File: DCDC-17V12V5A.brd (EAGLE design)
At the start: 40 x 23 mm, 36 parts, among them CN2 2828XX-2282834-2, CN3 2828XX-2282834-2, Q10 NMOSFET, Q9 NMOSFET, U1 LM3150MHX/NOPB

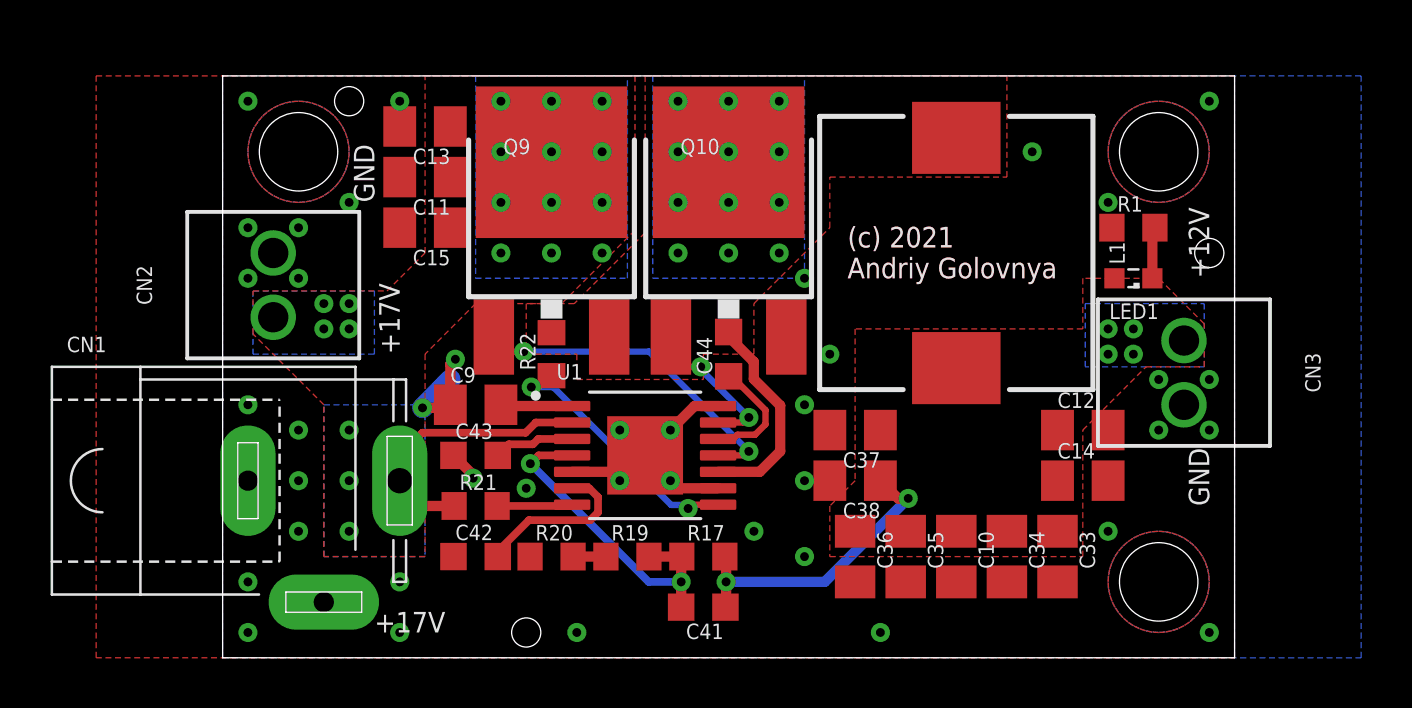
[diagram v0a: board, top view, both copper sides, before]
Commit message: Improved layout of DC-DC board. Rotated input terminal. Generated CAM files. Generated BoM and PnP files. Generated PNG preview. Generated PDF schematics.
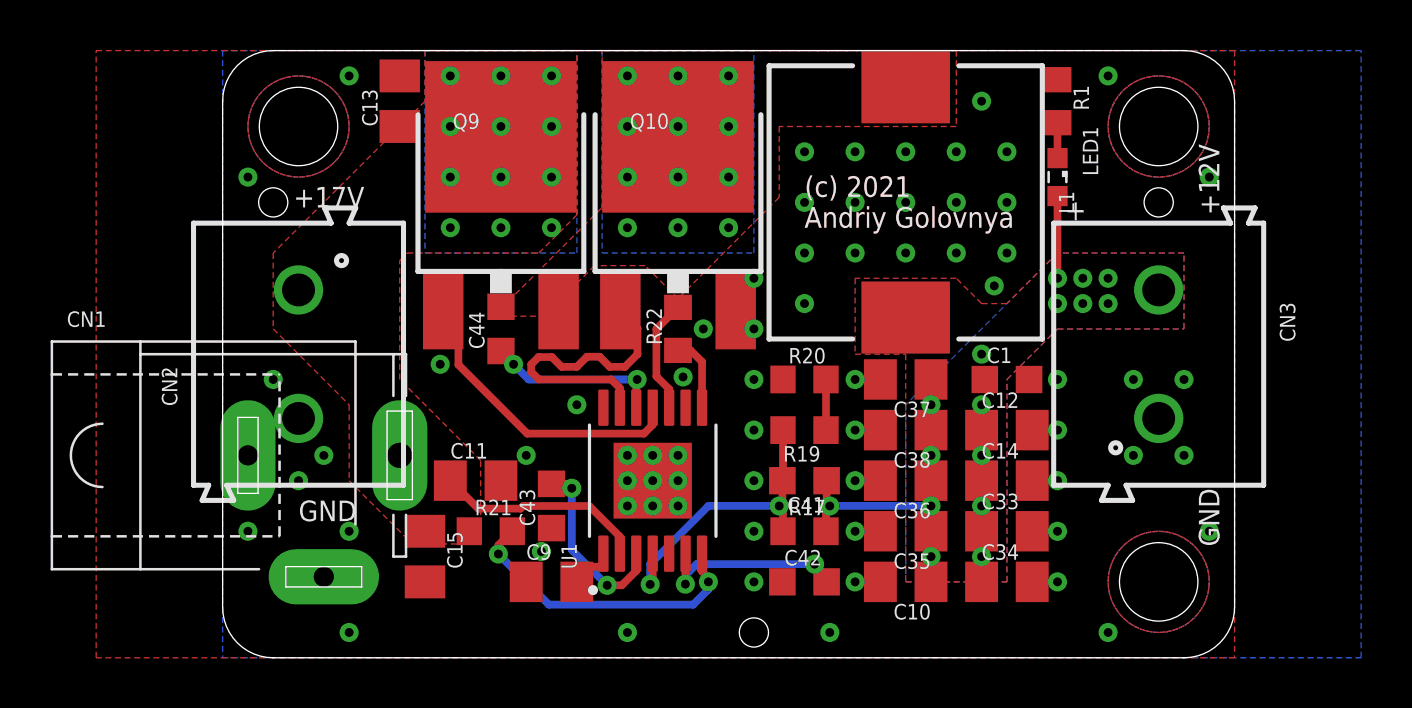
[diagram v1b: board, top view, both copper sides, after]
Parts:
- added C1: 1nF, rcl:C0603K
- CN2, CN3: value 2828XX-2282834-2 -> (none); device Connector:TERMBLK_254-2N -> Wurth_Connectors_WR-TBL Rising Cage Clamp:691213510002
- moved C42 13.0 mm to (23.0, 3.00)
- moved C15 13.0 mm to (8.00, 4.00), turned to 270 degrees
- moved R20 12.2 mm to (23.0, 11.0)
- moved C11 12.2 mm to (10.0, 7.00), turned to 0 degrees
- moved C44 9.06 mm to (11.0, 13.0)
- moved HOLE3 9.00 mm to (21.0, 1.00)
- moved R19 8.60 mm to (23.0, 9.00), turned to 180 degrees
- moved C9 7.62 mm to (13.0, 3.00)
- moved C41 6.40 mm to (23.0, 7.00)
- moved R1 5.83 mm to (33.0, 22.0), turned to 270 degrees
- moved R22 5.10 mm to (18.0, 13.0)
- moved HOLE2 5.00 mm to (2.00, 18.0)
- moved LED1 5.00 mm to (33.0, 19.0), turned to 270 degrees
- moved CN2 4.12 mm to (3.00, 12.0)
- moved R17 4.12 mm to (23.0, 5.00)
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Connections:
- net N$16 renamed BUCK_SS
- net N$18 renamed BUCK_EN
- net N$19 renamed BUCK_VCC
- net N$21 renamed BUCK_RON
- net N$23 renamed BUCK_BST
- net N$8 renamed BUCK_ILIM
- removed net 12V: C10.1, C12.1, C14.1, C33.1, C34.1, C35.1, C36.1, C37.1, C38.1, C41.1, CN3.2, L1.2, LED1.A, R17.2
- new net 5V: C1.1, C10.1, C12.1, C14.1, C33.1, C34.1, C35.1, C36.1, C37.1, C38.1, C41.1, CN3.2, L1.2, LED1.A, R17.2
- net GND: now also C1.2, CN2.2; no longer CN2.1
- net VIN: now also CN2.1; no longer CN2.2
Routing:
- net GND: track 12.1 -> 0.00 mm, vias 40 -> 69
- net 12V: track 12.0 -> 0.00 mm, vias 6 -> 0
- net 5V: track 0.00 -> 9.36 mm, vias 0 -> 16
- net BUCK_RON: track 2.99 -> 12.0 mm, vias 0 -> 2
- net BUCK_ILIM: track 10.4 -> 2.95 mm, vias 2 -> 0
- net BUCK_LG: track 6.23 -> 11.8 mm, vias 2 -> 0
- net BUCK_EN: track 3.21 -> 7.35 mm, vias 0 -> 2
- net BUCK_SW: track 8.35 -> 4.53 mm
- net VIN: track 10.9 -> 8.38 mm, vias 19 -> 12
- net BUCK_BST: track 4.68 -> 6.99 mm, vias 0 -> 2
- net BUCK_HG: track 13.3 -> 12.0 mm, vias 2 -> 0
- net BUCK_SS: track 6.58 -> 7.75 mm, vias 0 -> 2
- net BUCK_VCC: track 2.84 -> 1.73 mm
- net BUCK_FB: track 13.0 -> 12.2 mm
- net N$2: track 1.30 -> 2.00 mm
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- added copper zone on layer 1, net 5V
- added copper zone on layer 16, net 5V
- removed copper zone on layer 1, net 12V
- removed copper zone on layer 16, net 12V
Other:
- board size 40 x 23 mm -> 40 x 24 mm
- board text added: "+"
- board text added: "DCDC-17V12V5A-0011"
- board text removed: "DCDC-17V12V5A-0010"

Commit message: Added proper voltage symbols on 3.3v and 12v boards. Generated PDF schematics.
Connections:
- net 5V renamed 12V
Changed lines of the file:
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@@
 <drawing>
 <settings>
-<setting alwaysvectorfont="yes"/>
+<setting alwaysvectorfont="no"/>
 <setting verticaltext="up"/>
 </settings>
@@
 <via x="29" y="18" extent="1-16" drill="0.35"/>
 </signal>
-<signal name="5V" airwireshidden="yes">
+<signal name="12V" airwireshidden="yes">
 <contactref element="C34" pad="1"/>
 <contactref element="C36" pad="1"/>
@@
 <via x="30" y="12" extent="1-16" drill="0.35"/>
 <wire x1="33" y1="18.25" x2="33" y2="15" width="0.3048" layer="1"/>
+<wire x1="35" y1="15" x2="37" y2="14.54" width="0" layer="19" extent="1-1"/>
+<wire x1="35" y1="14" x2="35" y2="15" width="0" layer="19" extent="1-1"/>
+<wire x1="34" y1="15" x2="35" y2="15" width="0" layer="19" extent="1-1"/>
+<wire x1="34" y1="14" x2="35" y2="14" width="0" layer="19" extent="1-1"/>
+<wire x1="33" y1="14" x2="34" y2="14" width="0" layer="19" extent="1-1"/>
+<wire x1="33" y1="15" x2="34" y2="15" width="0" layer="19" extent="1-1"/>
+<wire x1="30" y1="12" x2="33" y2="14" width="0" layer="19" extent="1-1"/>
+<wire x1="30.125" y1="11" x2="30" y2="12" width="0" layer="19" extent="1-1"/>
+<wire x1="30" y1="10" x2="30.125" y2="11" width="0" layer="19" extent="1-1"/>
+<wire x1="30" y1="9" x2="30" y2="10" width="0" layer="19" extent="1-1"/>
+<wire x1="30" y1="8" x2="30" y2="9" width="0" layer="19" extent="1-1"/>
+<wire x1="30" y1="7" x2="30" y2="8" width="0" layer="19" extent="1-1"/>
+<wire x1="30" y1="6" x2="30" y2="7" width="0" layer="19" extent="1-1"/>
+<wire x1="30" y1="5" x2="30" y2="6" width="0" layer="19" extent="1-1"/>
+<wire x1="30" y1="4" x2="30" y2="5" width="0" layer="19" extent="1-1"/>
+<wire x1="30" y1="3" x2="30" y2="4" width="0" layer="19" extent="1-1"/>
+<wire x1="28" y1="9" x2="30" y2="9" width="0" layer="19" extent="1-1"/>
+<wire x1="28" y1="10" x2="28" y2="9" width="0" layer="19" extent="1-1"/>
+<wire x1="28" y1="11" x2="28" y2="10" width="0" layer="19" extent="1-1"/>
+<wire x1="28" y1="8" x2="28" y2="9" width="0" layer="19" extent="1-1"/>
+<wire x1="28" y1="7" x2="28" y2="8" width="0" layer="19" extent="1-1"/>
+<wire x1="28" y1="6" x2="28" y2="7" width="0" layer="19" extent="1-1"/>
+<wire x1="28" y1="5" x2="28" y2="6" width="0" layer="19" extent="1-1"/>
+<wire x1="28" y1="4" x2="28" y2="5" width="0" layer="19" extent="1-1"/>
+<wire x1="28" y1="3" x2="28" y2="4" width="0" layer="19" extent="1-1"/>
+<wire x1="27" y1="13.45" x2="28" y2="11" width="0" layer="19" extent="1-1"/>
 </signal>
 <signal name="BUCK_LG">

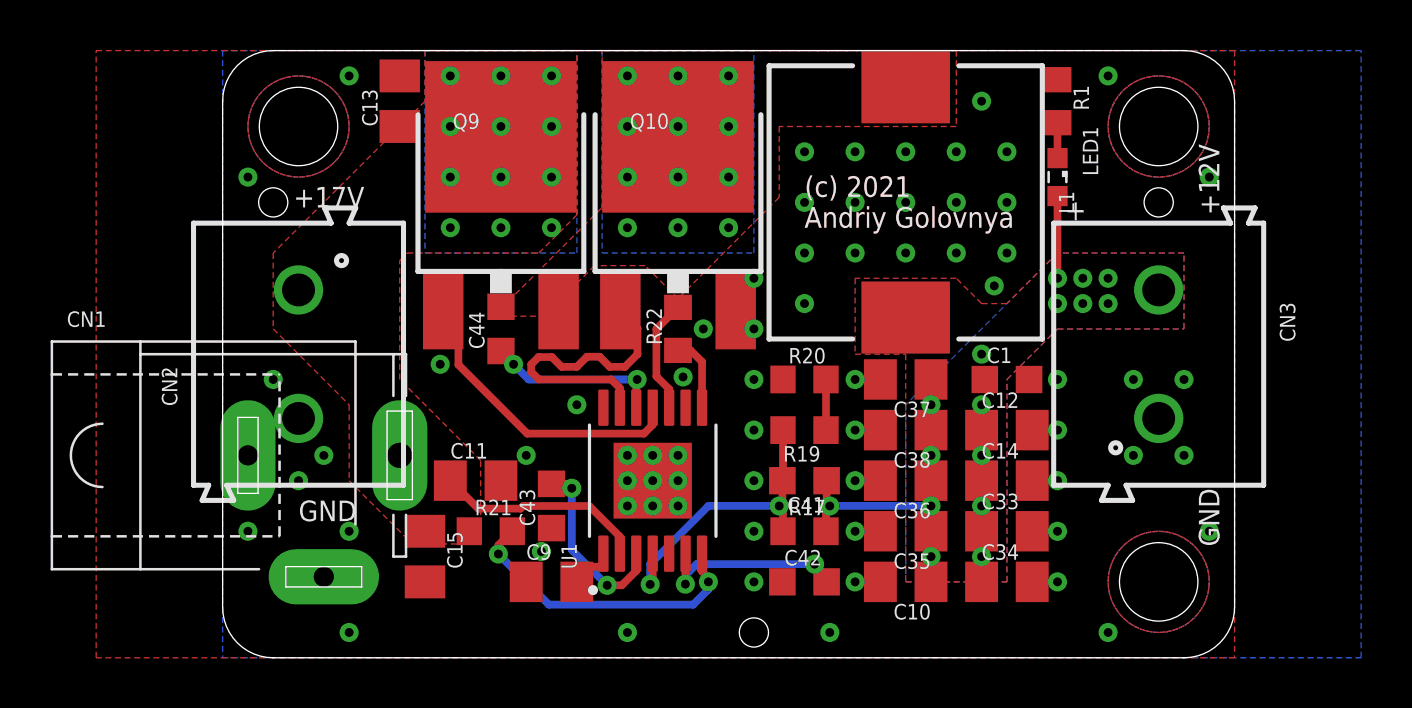
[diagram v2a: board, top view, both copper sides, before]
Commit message: Moved some texts and tooling holes a bit. Generated CAM files. Generated PNG preview. Generated PDF schematics. Renamed BoM and PnP files.
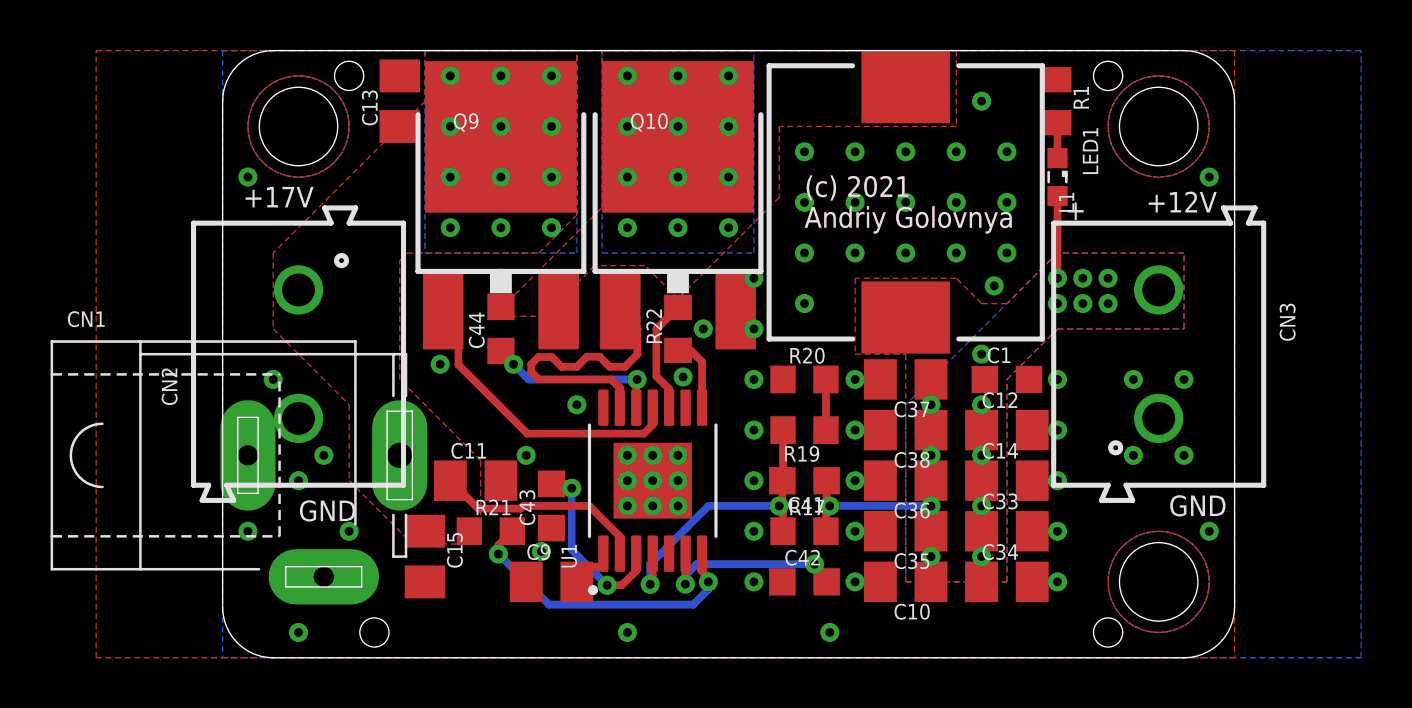
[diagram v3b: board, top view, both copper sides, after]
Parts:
- added HOLE4: TOOLINGHOLE, _my_fiducia:TOOLING-HOLE
- moved HOLE3 15.0 mm to (6.00, 1.00)
- moved HOLE2 5.83 mm to (5.00, 23.0)
- moved HOLE1 5.39 mm to (35.0, 23.0)
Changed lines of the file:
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@@
 <hole x="37" y="3" drill="3.1"/>
 <text x="33" y="20" size="1.6764" layer="22" font="vector" ratio="20" rot="MR0">DCDC-17V12V5A-0011</text>
-<text x="2.8" y="17.8" size="0.8128" layer="21" font="vector">+17V</text>
+<text x="0.8" y="17.8" size="0.8128" layer="21" font="vector">+17V</text>
 <text x="3" y="5.4" size="0.8128" layer="21" font="vector">GND</text>
-<text x="39.4" y="4.4" size="0.8128" layer="21" font="vector" rot="R90">GND</text>
-<text x="39.4" y="17.5" size="0.8128" layer="21" font="vector" rot="R90">+12V</text>
+<text x="37.4" y="5.6" size="0.8128" layer="21" font="vector">GND</text>
+<text x="36.5" y="17.6" size="0.8128" layer="21" font="vector">+12V</text>
 <text x="33" y="16" size="1.27" layer="22" font="vector" rot="MR0">(c) Andriy Golovnya</text>
 <text x="33" y="18" size="1.27" layer="22" font="vector" rot="MR0">12V/5A DC-DC Buck Converter</text>
@@
 <attribute name="VALUE" x="31.095" y="22.635" size="0.6096" layer="27" font="vector" rot="R270"/>
 </element>
-<element name="HOLE1" library="_my_fiducia" package="TOOLING-HOLE" value="TOOLINGHOLE" x="37" y="18" smashed="yes"/>
-<element name="HOLE2" library="_my_fiducia" package="TOOLING-HOLE" value="TOOLINGHOLE" x="2" y="18" smashed="yes"/>
-<element name="HOLE3" library="_my_fiducia" package="TOOLING-HOLE" value="TOOLINGHOLE" x="21" y="1" smashed="yes"/>
+<element name="HOLE1" library="_my_fiducia" package="TOOLING-HOLE" value="TOOLINGHOLE" x="35" y="23" smashed="yes"/>
+<element name="HOLE2" library="_my_fiducia" package="TOOLING-HOLE" value="TOOLINGHOLE" x="5" y="23" smashed="yes"/>
+<element name="HOLE3" library="_my_fiducia" package="TOOLING-HOLE" value="TOOLINGHOLE" x="6" y="1" smashed="yes"/>
 <element name="C1" library="rcl" library_urn="urn:adsk.eagle:library:334" package="C0603K" package3d_urn="urn:adsk.eagle:package:23680/2" value="1nF" x="31" y="11" smashed="yes">
 <attribute name="NAME" x="30.2" y="11.65" size="0.6096" layer="25" font="vector"/>
@@
 <attribute name="VALUE" x="30.2" y="9.35" size="0.6096" layer="27" font="vector"/>
 </element>
+<element name="HOLE4" library="_my_fiducia" package="TOOLING-HOLE" value="TOOLINGHOLE" x="35" y="1" smashed="yes"/>
 </elements>
 <signals>
@@
 <via x="33" y="5" extent="1-16" drill="0.35"/>
 <via x="33" y="3" extent="1-16" drill="0.35"/>
-<via x="5" y="23" extent="1-16" drill="0.35"/>
 <via x="30.5" y="14.7" extent="1-16" drill="0.35"/>
 <via x="30" y="22" extent="1-16" drill="0.35"/>
-<via x="35" y="23" extent="1-16" drill="0.35"/>
 <via x="39" y="19" extent="1-16" drill="0.35"/>
 <via x="39" y="5" extent="1-16" drill="0.35"/>
@@
 <via x="1" y="5" extent="1-16" drill="0.35"/>
 <via x="1" y="19" extent="1-16" drill="0.35"/>
-<via x="35" y="1" extent="1-16" drill="0.35"/>
 <via x="17" y="8" extent="1-16" drill="0.35"/>
 <via x="17" y="7" extent="1-16" drill="0.35"/>
@@
 <via x="4" y="8" extent="1-16" drill="0.35"/>
 <via x="2" y="11" extent="1-16" drill="0.35"/>
-<via x="5" y="1" extent="1-16" drill="0.35"/>
+<via x="3" y="1" extent="1-16" drill="0.35"/>
 <via x="12" y="8" extent="1-16" drill="0.35"/>
 <via x="12.6" y="4.2" extent="1-16" drill="0.35"/>
@@
 <via x="30" y="12" extent="1-16" drill="0.35"/>
 <wire x1="33" y1="18.25" x2="33" y2="15" width="0.3048" layer="1"/>
-<wire x1="35" y1="15" x2="37" y2="14.54" width="0" layer="19" extent="1-1"/>
-<wire x1="35" y1="14" x2="35" y2="15" width="0" layer="19" extent="1-1"/>
-<wire x1="34" y1="15" x2="35" y2="15" width="0" layer="19" extent="1-1"/>
-<wire x1="34" y1="14" x2="35" y2="14" width="0" layer="19" extent="1-1"/>
-<wire x1="33" y1="14" x2="34" y2="14" width="0" layer="19" extent="1-1"/>
-<wire x1="33" y1="15" x2="34" y2="15" width="0" layer="19" extent="1-1"/>
-<wire x1="30" y1="12" x2="33" y2="14" width="0" layer="19" extent="1-1"/>
-<wire x1="30.125" y1="11" x2="30" y2="12" width="0" layer="19" extent="1-1"/>
-<wire x1="30" y1="10" x2="30.125" y2="11" width="0" layer="19" extent="1-1"/>
-<wire x1="30" y1="9" x2="30" y2="10" width="0" layer="19" extent="1-1"/>
-<wire x1="30" y1="8" x2="30" y2="9" width="0" layer="19" extent="1-1"/>
-<wire x1="30" y1="7" x2="30" y2="8" width="0" layer="19" extent="1-1"/>
-<wire x1="30" y1="6" x2="30" y2="7" width="0" layer="19" extent="1-1"/>
-<wire x1="30" y1="5" x2="30" y2="6" width="0" layer="19" extent="1-1"/>
-<wire x1="30" y1="4" x2="30" y2="5" width="0" layer="19" extent="1-1"/>
-<wire x1="30" y1="3" x2="30" y2="4" width="0" layer="19" extent="1-1"/>
-<wire x1="28" y1="9" x2="30" y2="9" width="0" layer="19" extent="1-1"/>
-<wire x1="28" y1="10" x2="28" y2="9" width="0" layer="19" extent="1-1"/>
-<wire x1="28" y1="11" x2="28" y2="10" width="0" layer="19" extent="1-1"/>
-<wire x1="28" y1="8" x2="28" y2="9" width="0" layer="19" extent="1-1"/>
-<wire x1="28" y1="7" x2="28" y2="8" width="0" layer="19" extent="1-1"/>
-<wire x1="28" y1="6" x2="28" y2="7" width="0" layer="19" extent="1-1"/>
-<wire x1="28" y1="5" x2="28" y2="6" width="0" layer="19" extent="1-1"/>
-<wire x1="28" y1="4" x2="28" y2="5" width="0" layer="19" extent="1-1"/>
-<wire x1="28" y1="3" x2="28" y2="4" width="0" layer="19" extent="1-1"/>
-<wire x1="27" y1="13.45" x2="28" y2="11" width="0" layer="19" extent="1-1"/>
 </signal>
 <signal name="BUCK_LG">

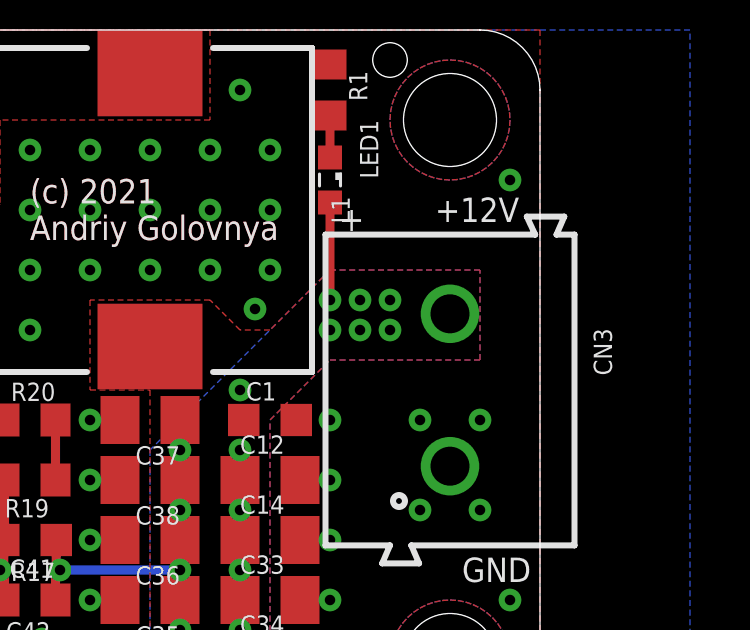
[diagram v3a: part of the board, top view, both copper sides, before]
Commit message: Added few vias. Generated CAM files. Generated PNG preview. Renamed BoM and PnP files.
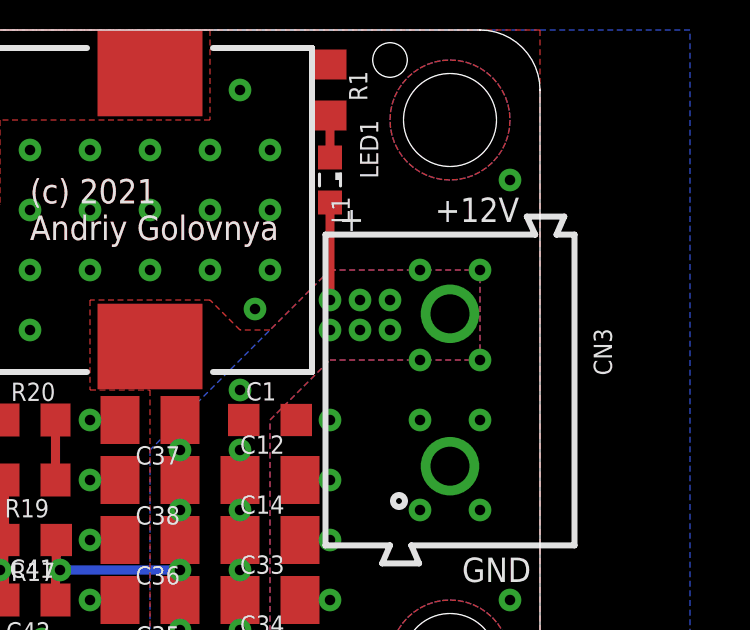
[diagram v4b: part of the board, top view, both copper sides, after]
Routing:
- net 12V: vias 16 -> 20
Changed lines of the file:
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@@
 <drawing>
 <settings>
-<setting alwaysvectorfont="no"/>
+<setting alwaysvectorfont="yes"/>
 <setting verticaltext="up"/>
 </settings>
@@
 <via x="30" y="12" extent="1-16" drill="0.35"/>
 <wire x1="33" y1="18.25" x2="33" y2="15" width="0.3048" layer="1"/>
+<via x="38" y="16" extent="1-16" drill="0.35"/>
+<via x="36" y="16" extent="1-16" drill="0.35"/>
+<via x="36" y="13" extent="1-16" drill="0.35"/>
+<via x="38" y="13" extent="1-16" drill="0.35"/>
 </signal>
 <signal name="BUCK_LG">
